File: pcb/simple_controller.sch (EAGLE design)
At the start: 68 parts, among them CON1 BINDER-IP40, CON2 BINDER-IP40, IC1 LD1117S50C, IC2 ST2378E, IC3 MCP1802, IC4 INA196, IC5 INA196, IC6 ATSAMC21G, Q1 24MHz, Q2 32768kHz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

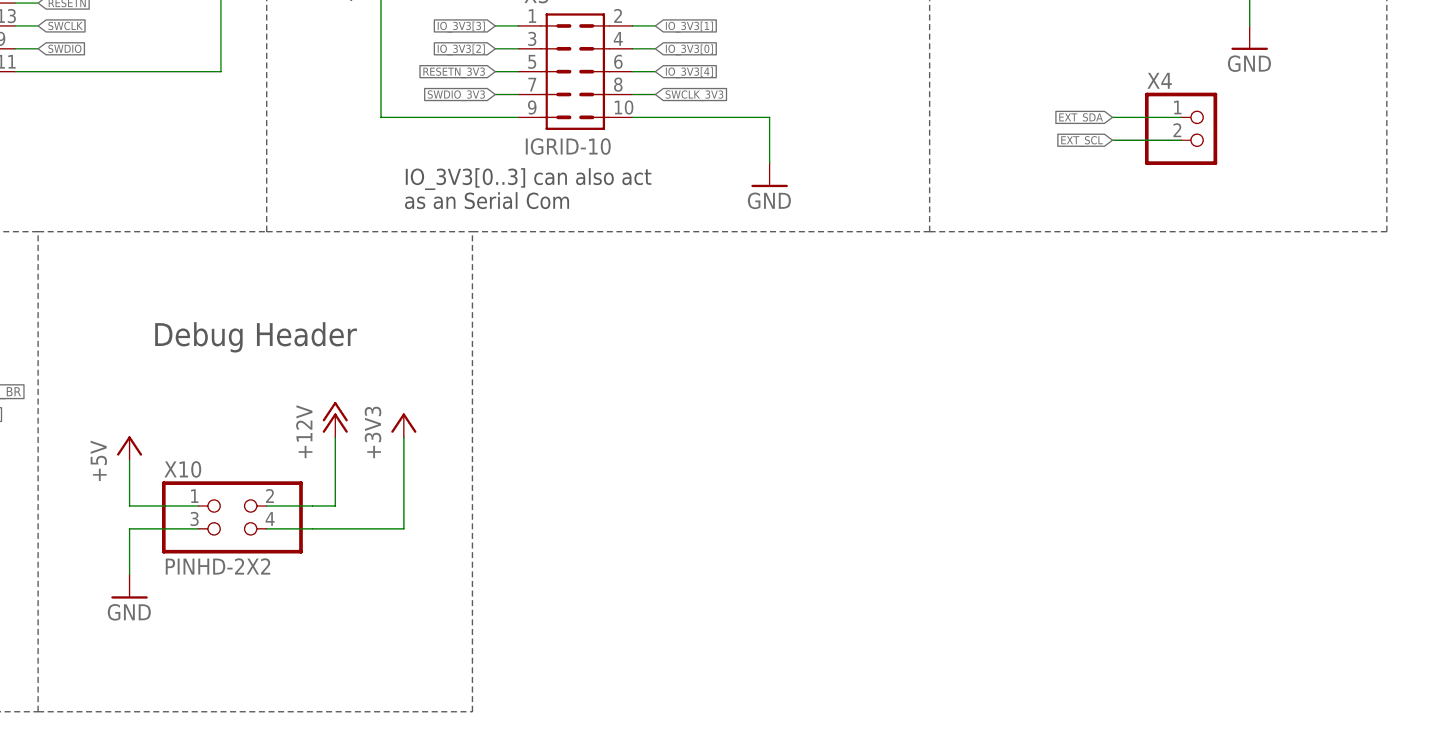
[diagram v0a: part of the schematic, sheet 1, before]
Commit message: reworked current path on boards and added new gerber files
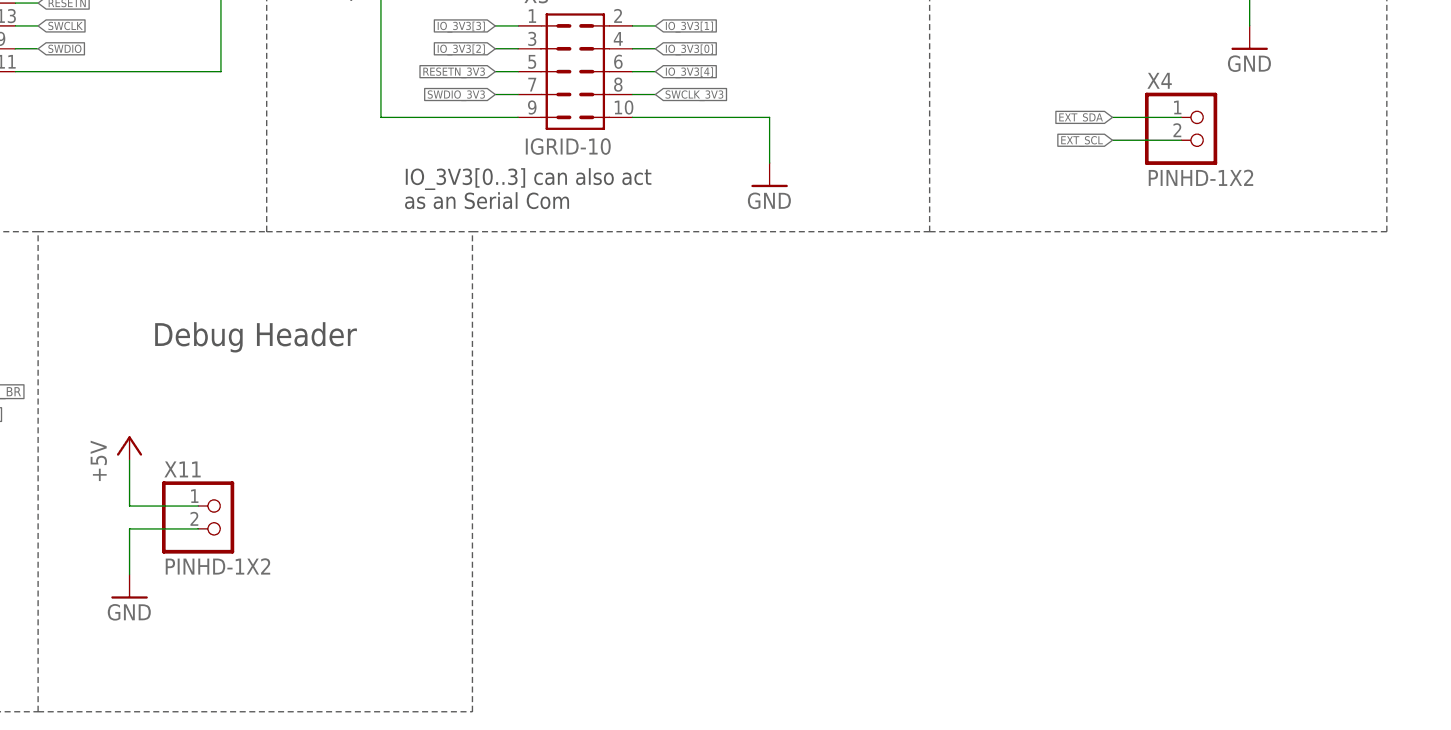
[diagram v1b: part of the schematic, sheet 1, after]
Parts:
- removed X10: PINHD-2X2, solderpi:PINHD-2X2
- added X11: PINHD-1X2, solderpi:PINHD-1X2
- X4, X6: value (none) -> PINHD-1X2
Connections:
- net +12V: no longer X10.2
- net +3V3: no longer X10.4
- net +5V: now also X11.1; no longer X10.1
- net GND: now also X11.2; no longer X10.3
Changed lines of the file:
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@@
 <?xml version="1.0" encoding="utf-8"?>
 <!DOCTYPE eagle SYSTEM "eagle.dtd">
-<eagle version="9.0.0">
+<eagle version="9.0.1">
 <drawing>
 <settings>
@@
 </part>
 <part name="GND21" library="supply1" library_urn="urn:adsk.eagle:library:371" deviceset="GND" device=""/>
-<part name="Q2" library="solderpi" library_urn="urn:adsk.eagle:library:1437534" deviceset="9HT11" device="" package3d_urn="urn:adsk.eagle:package:2669386/1" value="32768kHz">
+<part name="Q2" library="solderpi" library_urn="urn:adsk.eagle:library:1437534" deviceset="9HT11" device="" package3d_urn="urn:adsk.eagle:package:2669386/2" value="32768kHz">
 <attribute name="OC_MOUSER" value="717-9HT11-32.7KDZC-T"/>
 </part>
@@
 </part>
 <part name="P+10" library="supply1" library_urn="urn:adsk.eagle:library:371" deviceset="+5V" device=""/>
-<part name="X1" library="solderpi" library_urn="urn:adsk.eagle:library:1437534" deviceset="NANOFIT-2" device="" package3d_urn="urn:adsk.eagle:package:2885802/1">
+<part name="X1" library="solderpi" library_urn="urn:adsk.eagle:library:1437534" deviceset="NANOFIT-2" device="" package3d_urn="urn:adsk.eagle:package:2885802/2">
 <attribute name="OC_MOUSER" value="538-105313-2102; 538-105325-1002; 538-105307-1202"/>
 </part>
@@
 <part name="P+9" library="supply1" library_urn="urn:adsk.eagle:library:371" deviceset="+12V" device=""/>
 <part name="P+7" library="supply1" library_urn="urn:adsk.eagle:library:371" deviceset="+12V" device=""/>
-<part name="C1" library="solderpi" library_urn="urn:adsk.eagle:library:1437534" deviceset="C-EEEFK" device="" package3d_urn="urn:adsk.eagle:package:2885805/1" value="470µF">
+<part name="C1" library="solderpi" library_urn="urn:adsk.eagle:library:1437534" deviceset="C-EEEFK" device="" package3d_urn="urn:adsk.eagle:package:2885805/2" value="470µF">
 <attribute name="OC_MOUSER" value="667-EEE-FK1E471P"/>
 </part>
@@
 <attribute name="OC_MOUSER" value="81-GRM155R61C105MA2D"/>
 </part>
-<part name="P+18" library="supply1" library_urn="urn:adsk.eagle:library:371" deviceset="+12V" device=""/>
-<part name="+3V1" library="supply1" library_urn="urn:adsk.eagle:library:371" deviceset="+3V3" device=""/>
 <part name="GND23" library="supply1" library_urn="urn:adsk.eagle:library:371" deviceset="GND" device=""/>
 <part name="P+19" library="supply1" library_urn="urn:adsk.eagle:library:371" deviceset="+5V" device=""/>
-<part name="X10" library="solderpi" library_urn="urn:adsk.eagle:library:1437534" deviceset="PINHD-2X2" device="" package3d_urn="urn:adsk.eagle:package:22455/2">
-<attribute name="OC_MOUSER" value="571-5-146254-2"/>
-</part>
 <part name="IC3" library="solderpi" library_urn="urn:adsk.eagle:library:1437534" deviceset="MCP1802" device="" package3d_urn="urn:adsk.eagle:package:1437676/7"/>
+<part name="X11" library="solderpi" library_urn="urn:adsk.eagle:library:1437534" deviceset="PINHD-1X2" device="" package3d_urn="urn:adsk.eagle:package:22435/2">
+<attribute name="OC_MOUSER" value="855-M20-9990246"/>
+</part>
 </parts>
 <sheets>
@@
 <attribute name="OC_MOUSER" x="15.24" y="88.9" size="0.889" layer="96" display="off"/>
 </instance>
-<instance part="P+18" gate="1" x="137.16" y="38.1"/>
-<instance part="+3V1" gate="G$1" x="144.78" y="38.1"/>
 <instance part="GND23" gate="1" x="114.3" y="17.78"/>
 <instance part="P+19" gate="1" x="114.3" y="35.56"/>
-<instance part="X10" gate="A" x="127" y="25.4">
-<attribute name="OC_MOUSER" x="127" y="25.4" size="0.889" layer="96" display="off"/>
-</instance>
 <instance part="IC3" gate="G$1" x="134.62" y="152.4"/>
+<instance part="X11" gate="G$1" x="124.46" y="25.4">
+<attribute name="OC_MOUSER" x="124.46" y="25.4" size="2.54" layer="96" display="off"/>
+</instance>
 </instances>
 <busses>
@@
 <segment>
 <pinref part="GND23" gate="1" pin="GND"/>
+<wire x1="114.3" y1="25.4" x2="114.3" y2="20.32" width="0.1524" layer="91"/>
+<pinref part="X11" gate="G$1" pin="2"/>
 <wire x1="121.92" y1="25.4" x2="114.3" y2="25.4" width="0.1524" layer="91"/>
-<wire x1="114.3" y1="25.4" x2="114.3" y2="20.32" width="0.1524" layer="91"/>
-<pinref part="X10" gate="A" pin="3"/>
 </segment>
 </net>
@@
 </segment>
 <segment>
-<wire x1="121.92" y1="27.94" x2="114.3" y2="27.94" width="0.1524" layer="91"/>
 <pinref part="P+19" gate="1" pin="+5V"/>
 <wire x1="114.3" y1="33.02" x2="114.3" y2="27.94" width="0.1524" layer="91"/>
-<pinref part="X10" gate="A" pin="1"/>
+<pinref part="X11" gate="G$1" pin="1"/>
+<wire x1="121.92" y1="27.94" x2="114.3" y2="27.94" width="0.1524" layer="91"/>
 </segment>
 </net>
@@
 <pinref part="IC1" gate="G$1" pin="IN"/>
 </segment>
-<segment>
-<wire x1="129.54" y1="27.94" x2="134.62" y2="27.94" width="0.1524" layer="91"/>
-<pinref part="P+18" gate="1" pin="+12V"/>
-<wire x1="134.62" y1="27.94" x2="137.16" y2="27.94" width="0.1524" layer="91"/>
-<wire x1="137.16" y1="27.94" x2="137.16" y2="35.56" width="0.1524" layer="91"/>
-<pinref part="X10" gate="A" pin="2"/>
-</segment>
 </net>
 <net name="+3V3" class="0">
@@
 <wire x1="157.48" y1="71.12" x2="142.24" y2="71.12" width="0.1524" layer="91"/>
 </segment>
-<segment>
-<wire x1="129.54" y1="25.4" x2="134.62" y2="25.4" width="0.1524" layer="91"/>
-<pinref part="+3V1" gate="G$1" pin="+3V3"/>
-<wire x1="144.78" y1="35.56" x2="144.78" y2="25.4" width="0.1524" layer="91"/>
-<wire x1="144.78" y1="25.4" x2="134.62" y2="25.4" width="0.1524" layer="91"/>
-<pinref part="X10" gate="A" pin="4"/>
-</segment>
 </net>

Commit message: fixing op amp (iron,tweezer)
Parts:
- C2, C3, C4, C5: value 10µF -> 1µF
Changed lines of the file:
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@@
 <attribute name="OC_MOUSER" value="667-EEE-FK1E471P"/>
 </part>
-<part name="C2" library="rcl" library_urn="urn:adsk.eagle:library:334" deviceset="C-EU" device="C0805" package3d_urn="urn:adsk.eagle:package:23617/2" value="10µF">
+<part name="C2" library="rcl" library_urn="urn:adsk.eagle:library:334" deviceset="C-EU" device="C0805" package3d_urn="urn:adsk.eagle:package:23617/2" value="1µF">
 <spice>
 <pinmapping spiceprefix="C">
@@
 <attribute name="OC_MOUSER" value="81-GRM21BR61E106MA3L"/>
 </part>
-<part name="C3" library="rcl" library_urn="urn:adsk.eagle:library:334" deviceset="C-EU" device="C0805" package3d_urn="urn:adsk.eagle:package:23617/2" value="10µF">
+<part name="C3" library="rcl" library_urn="urn:adsk.eagle:library:334" deviceset="C-EU" device="C0805" package3d_urn="urn:adsk.eagle:package:23617/2" value="1µF">
 <spice>
 <pinmapping spiceprefix="C">
@@
 <attribute name="OC_MOUSER" value="81-GRM21BR61E106MA3L"/>
 </part>
-<part name="C4" library="rcl" library_urn="urn:adsk.eagle:library:334" deviceset="C-EU" device="C0805" package3d_urn="urn:adsk.eagle:package:23617/2" value="10µF">
+<part name="C4" library="rcl" library_urn="urn:adsk.eagle:library:334" deviceset="C-EU" device="C0805" package3d_urn="urn:adsk.eagle:package:23617/2" value="1µF">
 <spice>
 <pinmapping spiceprefix="C">
@@
 <attribute name="OC_MOUSER" value="81-GRM21BR61E106MA3L"/>
 </part>
-<part name="C5" library="rcl" library_urn="urn:adsk.eagle:library:334" deviceset="C-EU" device="C0805" package3d_urn="urn:adsk.eagle:package:23617/2" value="10µF">
+<part name="C5" library="rcl" library_urn="urn:adsk.eagle:library:334" deviceset="C-EU" device="C0805" package3d_urn="urn:adsk.eagle:package:23617/2" value="1µF">
 <spice>
 <pinmapping spiceprefix="C">

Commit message: parts reworked
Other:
- note added: "EXINT[9]"
- note removed: "EXINT[1]"
- note removed: "EXINT[2]"
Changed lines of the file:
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@@
 <?xml version="1.0" encoding="utf-8"?>
 <!DOCTYPE eagle SYSTEM "eagle.dtd">
-<eagle version="9.2.2">
+<eagle version="9.3.1">
 <drawing>
 <settings>
@@
 <text x="109.22" y="57.15" size="1.4224" layer="97">SERCOM3/PAD[3] \\ EXINT[13]</text>
 <text x="109.22" y="74.93" size="1.4224" layer="97">TCC0/WO[2]</text>
-<text x="53.34" y="72.39" size="1.4224" layer="97">EXINT[3]</text>
-<text x="53.34" y="74.93" size="1.4224" layer="97">EXINT[2]</text>
-<text x="53.34" y="77.47" size="1.4224" layer="97">EXINT[1]</text>
+<text x="53.34" y="72.39" size="1.4224" layer="97">EXINT[9]</text>
+<text x="53.34" y="74.93" size="1.4224" layer="97">EXINT[8]</text>
+<text x="53.34" y="77.47" size="1.4224" layer="97">EXINT[3]</text>
 <text x="53.34" y="80.01" size="1.4224" layer="97">EXINT[0]</text>
 <text x="109.22" y="46.99" size="1.4224" layer="97">EXINT[8]</text>
